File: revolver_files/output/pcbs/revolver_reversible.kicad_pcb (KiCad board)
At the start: 2 copper layers, 127.8 x 57.7 mm, 15 parts

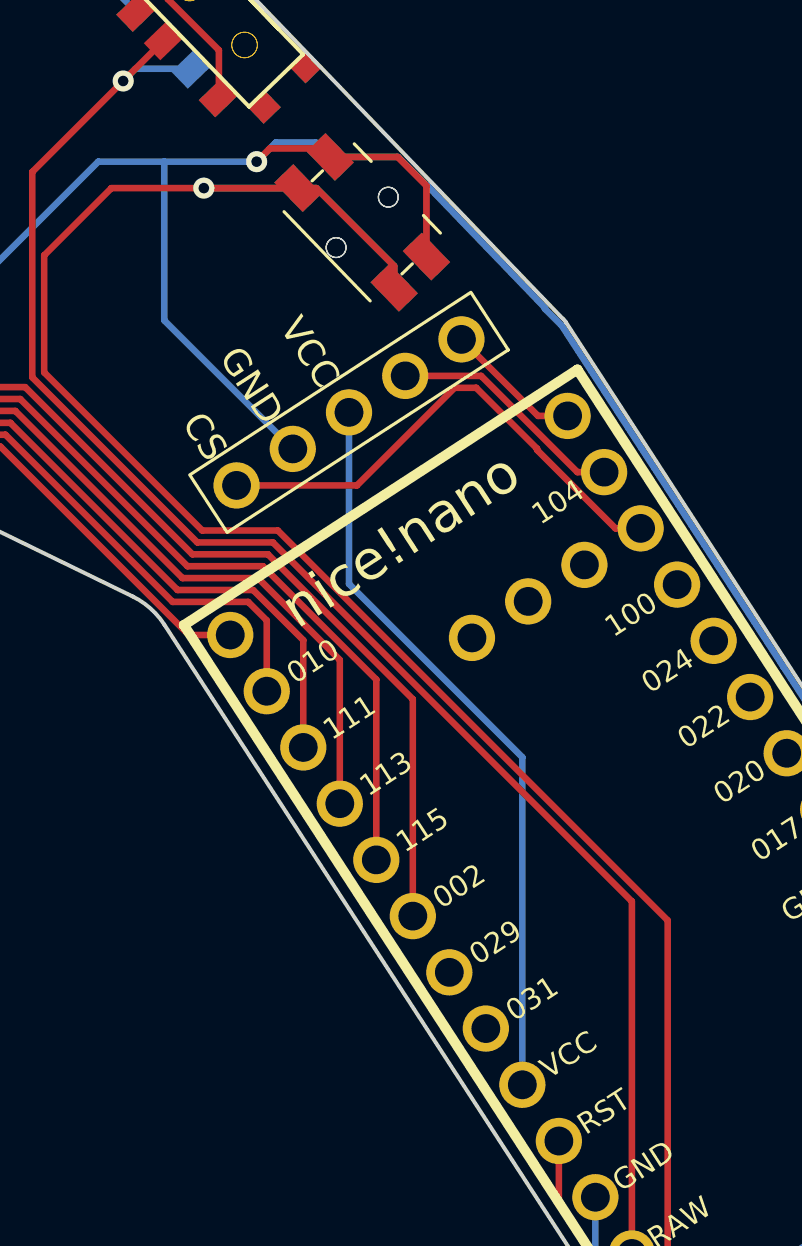
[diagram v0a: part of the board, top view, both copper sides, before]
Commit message: mucking about trying to make the niceview pins reversible
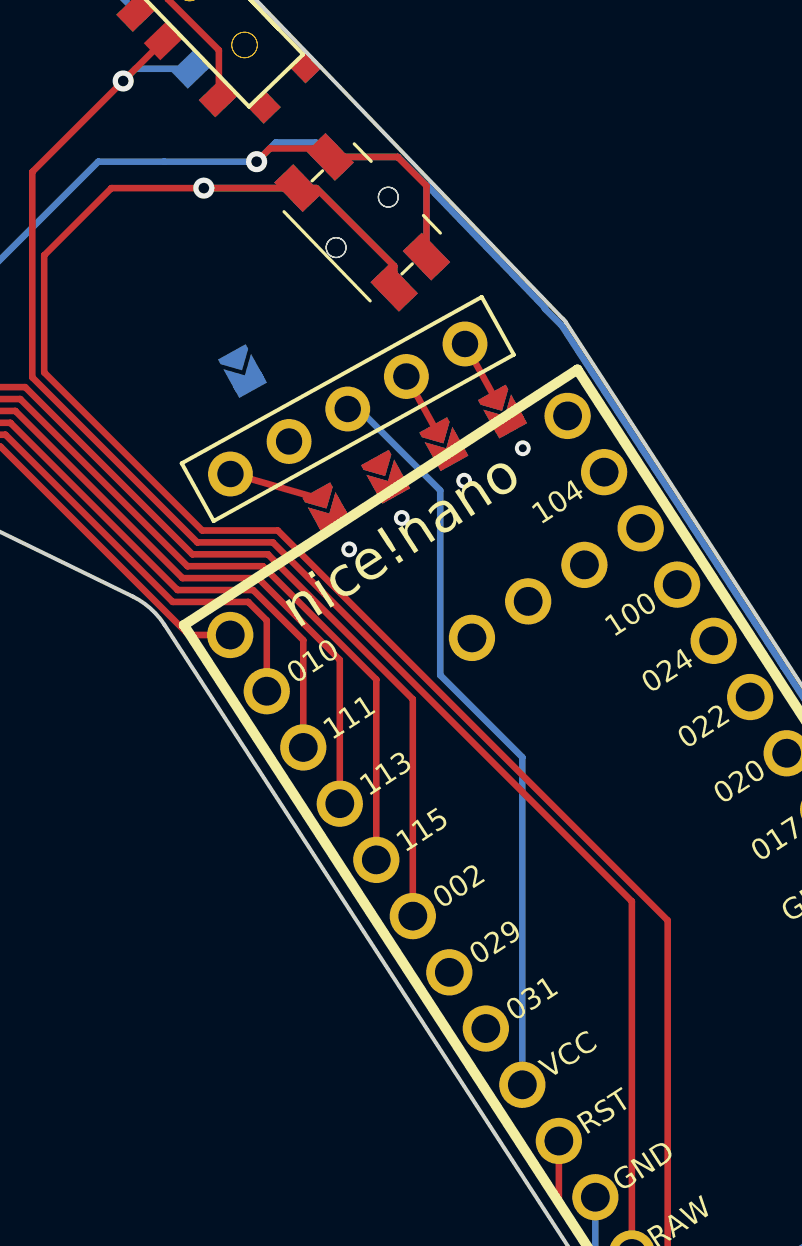
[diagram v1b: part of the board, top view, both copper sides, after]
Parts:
- removed Display2: nice!view, urchin-footprints:nice_view
- added J15, J24: Jumper, lib:Jumper, F.Cu at (196.4, 95.0)
- added J16, J23: Jumper, lib:Jumper, F.Cu at (194.1, 96.3)
- added J18: Jumper, lib:Jumper, F.Cu at (186.5, 93.5)
- added J18, J21: Jumper, lib:Jumper, F.Cu at (191.9, 97.5)
- added J19, J20: Jumper, lib:Jumper, F.Cu at (189.7, 98.7)
- added Nice!View1: , lib:niceview_headers, F.Cu at (190.5, 94.9)
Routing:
- net P011: track 19.1 -> 0.00 mm
- net GND: track 326.5 -> 313.6 mm
- net P104: track 9.05 -> 0.00 mm
- net P106: track 5.22 -> 0.00 mm, vias 0 -> 1
- net NN_CS_SDA: track 0.00 -> 3.59 mm
- net NN_SCL_GND: track 0.00 -> 2.50 mm
- net NN_SDA_CS: track 0.00 -> 2.50 mm
- net VCC: track 28.2 -> 28.6 mm, vias 0 -> 1
- net SCL: vias 0 -> 1
- net CS: vias 0 -> 1
